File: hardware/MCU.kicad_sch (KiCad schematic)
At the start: 0 parts

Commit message: Schematic for the MCU and Tag Connect
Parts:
- added C14: 100nF, symbol Device:C
- added C15: 4.7uF, symbol Device:C
- added J2: SWD Debug, symbol Connector_Generic:Conn_01x06
- added R5: 10k, symbol Device:R
- added SW1: SW_Push, symbol Switch:SW_Push
- added U3: STM32G071KBUxN, Package_DFN_QFN:QFN-32-1EP_5x5mm_P0.5mm_EP3.45x3.45mm, symbol MCU_ST_STM32G0:STM32G071KBUxN
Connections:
- new net: SW1.2, U3.6 (PF2)
- new net: C14.2, C15.1
- new net 3V3: C14.1, J2.1 (Pin_1), U3.4 (VDD)
- new net EN_RAILB: U3.15 (PB0)
- new net GND: C15.2, J2.3 (Pin_3), J2.5 (Pin_5), R5.2, SW1.1, U3.33 (VSS), U3.5 (VSS)
- new net I2C1_SCL: U3.19 (PA9/UCPD1_DBCC1)
- new net I2C1_SDA: U3.21 (PA10/UCPD1_DBCC2)
- new net SWCLK_BOOT0: J2.4 (Pin_4), R5.1, U3.25 (PA14)
- new net SWDIO: J2.2 (Pin_2), U3.24 (PA13)
- new net USART2_RX: U3.10 (PA3)
- new net USART2_TX: U3.9 (PA2)

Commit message: Schematics Completed
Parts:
- removed J2: SWD Debug, symbol Connector_Generic:Conn_01x06

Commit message: Completed Schematic
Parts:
- added C16: 100nF, symbol Device:C
- added D2: STATUS_G, symbol Device:LED
- added D3: ERROR_R, symbol Device:LED
- added R10, R11: 470, symbol Device:R
- added R9: 10k, symbol Device:R
- renumbered R5 to R6
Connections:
- net 3V3: now also R9.2
- net GND: now also C16.2, D2.1 (K), D3.1 (K)
- net RESET: now reaches SW1.2, U3.6 (PF2)
- net RESET: now also C16.1, R9.1
- net at U3.12 (PA5): now also R10.1
- net at U3.13 (PA6): now also R11.1
- new net: D3.2 (A), R11.2
- new net: D2.2 (A), R10.2
- no-connect marks 0 -> 20
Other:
- moved on the sheet: C14, C15, R6, SW1, U3

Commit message: Assigned Footprints and Libraries
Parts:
- C14, C15, C16: footprint (none) -> Capacitor_SMD:C_0603_1608Metric
- D2, D3: footprint (none) -> LED_SMD:LED_0201_0603Metric
- R10, R11, R6, R9: footprint (none) -> Resistor_SMD:R_0201_0603Metric
- SW1: footprint (none) -> Button_Switch_SMD:SW_SPST_EVQP2_MiddlePushTravel_H2.5mm
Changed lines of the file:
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@@
 			)
 		)
-		(property "Footprint" ""
+		(property "Footprint" "Resistor_SMD:R_0201_0603Metric"
 			(at 188.722 113.03 90)
 			(hide yes)
@@
 			)
 		)
-		(property "Footprint" ""
+		(property "Footprint" "Resistor_SMD:R_0201_0603Metric"
 			(at 203.2 94.488 90)
 			(hide yes)
@@
 			)
 		)
-		(property "Footprint" ""
+		(property "Footprint" "Resistor_SMD:R_0201_0603Metric"
 			(at 203.2 84.328 90)
 			(hide yes)
@@
 			)
 		)
-		(property "Footprint" ""
+		(property "Footprint" "Button_Switch_SMD:SW_SPST_EVQP2_MiddlePushTravel_H2.5mm"
 			(at 102.87 68.58 0)
 			(hide yes)
@@
 			)
 		)
-		(property "Footprint" ""
+		(property "Footprint" "Capacitor_SMD:C_0603_1608Metric"
 			(at 172.72 54.9148 0)
 			(hide yes)
@@
 			)
 		)
-		(property "Footprint" ""
+		(property "Footprint" "Capacitor_SMD:C_0603_1608Metric"
 			(at 112.7252 82.55 0)
 			(hide yes)
@@
 			)
 		)
-		(property "Footprint" ""
+		(property "Footprint" "Resistor_SMD:R_0201_0603Metric"
 			(at 126.238 64.77 90)
 			(hide yes)
@@
 			)
 		)
-		(property "Footprint" ""
+		(property "Footprint" "Capacitor_SMD:C_0603_1608Metric"
 			(at 181.61 54.9148 0)
 			(hide yes)
@@
 			)
 		)
-		(property "Footprint" ""
+		(property "Footprint" "LED_SMD:LED_0201_0603Metric"
 			(at 212.09 82.55 0)
 			(hide yes)
@@
 			)
 		)
-		(property "Footprint" ""
+		(property "Footprint" "LED_SMD:LED_0201_0603Metric"
 			(at 212.09 92.71 0)
 			(hide yes)

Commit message: Update MCU with different enable pin
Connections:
- net EN_RAILB: now also U3.23 (PA10/PA12); no longer U3.15 (PB0)
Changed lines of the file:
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@@
-	)
-	(no_connect
-		(at 186.69 101.6)
 	)
 	(no_connect
@@
 	)
 	(no_connect
+		(at 135.89 101.6)
+	)
+	(no_connect
 		(at 135.89 104.14)
 	)
@@
 	(wire
 		(pts
-			(xy 190.5 100.33) (xy 190.5 99.06)
-		)
-		(stroke
-			(width 0)
-			(type default)
-		)
-	)
-	(wire
-		(pts
 			(xy 215.9 82.55) (xy 219.71 82.55)
 		)
@@
 	(wire
 		(pts
-			(xy 128.27 101.6) (xy 135.89 101.6)
-		)
-		(stroke
-			(width 0)
-			(type default)
-		)
-	)
-	(wire
-		(pts
 			(xy 111.76 74.93) (xy 111.76 73.66)
 		)
@@
 	(wire
 		(pts
-			(xy 190.5 100.33) (xy 195.58 100.33)
-		)
-		(stroke
-			(width 0)
-			(type default)
-		)
-	)
-	(wire
-		(pts
 			(xy 111.76 83.82) (xy 111.76 82.55)
 		)
@@
 	(wire
 		(pts
+			(xy 186.69 101.6) (xy 209.55 101.6)
+		)
+		(stroke
+			(width 0)
+			(type default)
+		)
+	)
+	(wire
+		(pts
 			(xy 207.01 92.71) (xy 208.28 92.71)
 		)
@@
 	(wire
 		(pts
-			(xy 186.69 99.06) (xy 190.5 99.06)
+			(xy 186.69 99.06) (xy 195.58 99.06)
 		)
 		(stroke
@@
 	(hierarchical_label "I2C1_SCL"
 		(shape input)
-		(at 195.58 100.33 0)
+		(at 195.58 99.06 0)
 		(effects
 			(font
@@
 		)
 	)
+	(hierarchical_label "EN_RAILB"
+		(shape input)
+		(at 209.55 101.6 0)
+		(effects
+			(font
+				(size 1.27 1.27)
+			)
+			(justify left)
+		)
+	)
 	(hierarchical_label "SWDIO"
 		(shape output)
@@
 		(effects
 			(font
-				(size 1.27 1.27)
-			)
-			(justify right)
-		)
-	)
-	(hierarchical_label "EN_RAILB"
-		(shape input)
-		(at 128.27 101.6 180)
-		(effects
-			(font

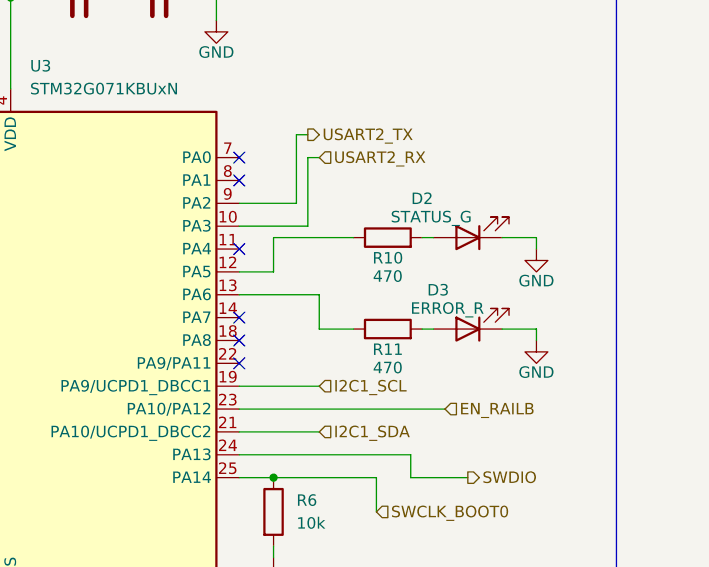
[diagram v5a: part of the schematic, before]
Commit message: LED circuit change
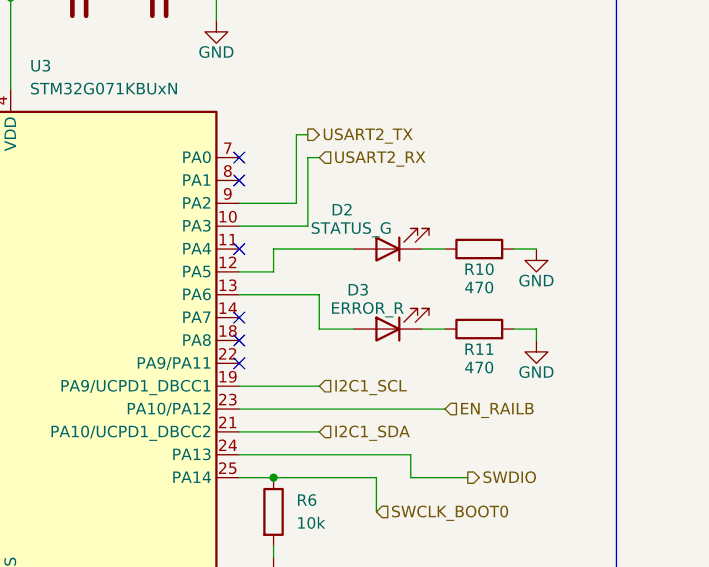
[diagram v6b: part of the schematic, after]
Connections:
- net GND: now also R10.2, R11.2; no longer D2.1 (K), D3.1 (K)
- net at R11.1: now also D3.1 (K); no longer U3.13 (PA6)
- net at D3.2 (A): now also U3.13 (PA6); no longer R11.2
- net at R10.1: now also D2.1 (K); no longer U3.12 (PA5)
- net at D2.2 (A): now also U3.12 (PA5); no longer R10.2
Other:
- moved on the sheet: R10, R11

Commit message: PCB V1.1
Board completed, updated with labels for external connectors. Corrected and tightened hot loop with better layout and routing
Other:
- moved on the sheet: D3, R11
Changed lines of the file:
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@@
 	(paper "A4")
 	(rectangle
-		(start 76.2 41.91)
-		(end 228.6 139.7)
+		(start 77.47 40.64)
+		(end 229.87 138.43)
 		(stroke
 			(width 0)
@@
 	(wire
 		(pts
+			(xy 190.5 88.9) (xy 186.69 88.9)
+		)
+		(stroke
+			(width 0)
+			(type default)
+		)
+	)
+	(wire
+		(pts
 			(xy 111.76 74.93) (xy 111.76 73.66)
 		)
@@
 	(wire
 		(pts
-			(xy 219.71 92.71) (xy 219.71 93.98)
+			(xy 219.71 91.44) (xy 219.71 92.71)
 		)
 		(stroke
@@
 	(wire
 		(pts
-			(xy 186.69 88.9) (xy 195.58 88.9)
-		)
-		(stroke
-			(width 0)
-			(type default)
-		)
-	)
-	(wire
-		(pts
 			(xy 212.09 109.22) (xy 205.74 109.22)
 		)
@@
 	(wire
 		(pts
-			(xy 207.01 92.71) (xy 209.55 92.71)
-		)
-		(stroke
-			(width 0)
-			(type default)
-		)
-	)
-	(wire
-		(pts
-			(xy 195.58 88.9) (xy 195.58 92.71)
+			(xy 207.01 91.44) (xy 209.55 91.44)
+		)
+		(stroke
+			(width 0)
+			(type default)
+		)
+	)
+	(wire
+		(pts
+			(xy 190.5 88.9) (xy 190.5 91.44)
 		)
 		(stroke
@@
 	(wire
 		(pts
-			(xy 217.17 92.71) (xy 219.71 92.71)
+			(xy 217.17 91.44) (xy 219.71 91.44)
 		)
 		(stroke
@@
 	(wire
 		(pts
-			(xy 194.31 73.66) (xy 194.31 81.28)
+			(xy 193.04 73.66) (xy 193.04 81.28)
 		)
 		(stroke
@@
 	(wire
 		(pts
+			(xy 219.71 85.09) (xy 219.71 83.82)
+		)
+		(stroke
+			(width 0)
+			(type default)
+		)
+	)
+	(wire
+		(pts
 			(xy 184.15 55.88) (xy 184.15 58.42)
 		)
@@
 	(wire
 		(pts
-			(xy 195.58 92.71) (xy 199.39 92.71)
-		)
-		(stroke
-			(width 0)
-			(type default)
-		)
-	)
-	(wire
-		(pts
-			(xy 193.04 78.74) (xy 186.69 78.74)
-		)
-		(stroke
-			(width 0)
-			(type default)
-		)
-	)
-	(wire
-		(pts
-			(xy 193.04 71.12) (xy 194.31 71.12)
-		)
-		(stroke
-			(width 0)
-			(type default)
-		)
-	)
-	(wire
-		(pts
-			(xy 193.04 71.12) (xy 193.04 78.74)
+			(xy 190.5 91.44) (xy 199.39 91.44)
+		)
+		(stroke
+			(width 0)
+			(type default)
+		)
+	)
+	(wire
+		(pts
+			(xy 191.77 78.74) (xy 186.69 78.74)
+		)
+		(stroke
+			(width 0)
+			(type default)
+		)
+	)
+	(wire
+		(pts
+			(xy 191.77 71.12) (xy 194.31 71.12)
+		)
+		(stroke
+			(width 0)
+			(type default)
+		)
+	)
+	(wire
+		(pts
+			(xy 191.77 71.12) (xy 191.77 78.74)
 		)
 		(stroke
@@
 	(wire
 		(pts
-			(xy 194.31 73.66) (xy 195.58 73.66)
+			(xy 193.04 73.66) (xy 195.58 73.66)
 		)
 		(stroke
@@
 	(wire
 		(pts
-			(xy 194.31 81.28) (xy 186.69 81.28)
-		)
-		(stroke
-			(width 0)
-			(type default)
-		)
-	)
-	(wire
-		(pts
-			(xy 217.17 83.82) (xy 219.71 83.82)
+			(xy 193.04 81.28) (xy 186.69 81.28)
+		)
+		(stroke
+			(width 0)
+			(type default)
+		)
+	)
+	(wire
+		(pts
+			(xy 219.71 83.82) (xy 217.17 83.82)
 		)
 		(stroke
@@
 	(symbol
 		(lib_id "Device:LED")
-		(at 203.2 92.71 180)
+		(at 203.2 91.44 180)
 		(unit 1)
 		(body_style 1)
@@
 		(dnp no)
 		(property "Reference" "D3"
-			(at 199.898 88.392 0)
+			(at 199.898 87.122 0)
 			(show_name no)
 			(do_not_autoplace no)
@@
 		)
 		(property "Value" "ERROR_R"
-			(at 200.914 90.424 0)
+			(at 200.914 89.154 0)
 			(show_name no)
 			(do_not_autoplace no)
@@
 		)
 		(property "Footprint" "LED_SMD:LED_0201_0603Metric"
-			(at 203.2 92.71 0)
+			(at 203.2 91.44 0)
 			(hide yes)
 			(show_name no)
@@
 		)
 		(property "Datasheet" ""
-			(at 203.2 92.71 0)
+			(at 203.2 91.44 0)
 			(hide yes)
 			(show_name no)
@@
 		)
 		(property "Description" "Light emitting diode"
-			(at 203.2 92.71 0)
+			(at 203.2 91.44 0)
 			(hide yes)
 			(show_name no)
@@
 		)
 		(property "Sim.Pins" "1=K 2=A"
-			(at 203.2 92.71 0)
+			(at 203.2 91.44 0)
 			(hide yes)
 			(show_name no)
@@
 	(symbol
 		(lib_id "power:GND")
-		(at 219.71 83.82 0)
+		(at 219.71 85.09 0)
 		(unit 1)
 		(body_style 1)
@@
 		(dnp no)
 		(property "Reference" "#PWR021"
-			(at 219.71 90.17 0)
+			(at 219.71 91.44 0)
 			(hide yes)
 			(show_name no)
@@
 		)
 		(property "Value" "GND"
-			(at 219.71 87.376 0)
+			(at 219.71 88.646 0)
 			(show_name no)
 			(do_not_autoplace no)
@@
 		)
 		(property "Footprint" ""
-			(at 219.71 83.82 0)
+			(at 219.71 85.09 0)
 			(hide yes)
 			(show_name no)
@@
 		)
 		(property "Datasheet" ""
-			(at 219.71 83.82 0)
+			(at 219.71 85.09 0)
 			(hide yes)
 			(show_name no)
@@
 		)
 		(property "Description" "Power symbol creates a global label with name \"GND\" , ground"
-			(at 219.71 83.82 0)
+			(at 219.71 85.09 0)
 			(hide yes)
 			(show_name no)
@@
 	(symbol
 		(lib_id "Device:R")
-		(at 213.36 92.71 90)
+		(at 213.36 91.44 90)
 		(unit 1)
 		(body_style 1)
@@
 		(dnp no)
 		(property "Reference" "R11"
-			(at 213.36 94.996 90)
+			(at 213.36 93.726 90)
 			(show_name no)
 			(do_not_autoplace no)
@@
 		)
 		(property "Value" "470"
-			(at 213.36 97.028 90)
+			(at 213.36 95.758 90)
 			(show_name no)
 			(do_not_autoplace no)
@@
 		)
 		(property "Footprint" "Resistor_SMD:R_0201_0603Metric"
-			(at 213.36 94.488 90)
+			(at 213.36 93.218 90)
 			(hide yes)
 			(show_name no)
@@
 		)
 		(property "Datasheet" ""
-			(at 213.36 92.71 0)
+			(at 213.36 91.44 0)
 			(hide yes)
 			(show_name no)
@@
 		)
 		(property "Description" "Resistor"
-			(at 213.36 92.71 0)
+			(at 213.36 91.44 0)
 			(hide yes)
 			(show_name no)
@@
 	(symbol
 		(lib_id "power:GND")
-		(at 219.71 93.98 0)
+		(at 219.71 92.71 0)
 		(unit 1)
 		(body_style 1)
@@
 		(dnp no)
 		(property "Reference" "#PWR022"
-			(at 219.71 100.33 0)
+			(at 219.71 99.06 0)
 			(hide yes)
 			(show_name no)
@@
 		)
 		(property "Value" "GND"
-			(at 219.71 97.536 0)
+			(at 219.71 96.266 0)
 			(show_name no)
 			(do_not_autoplace no)
@@
 		)
 		(property "Footprint" ""
-			(at 219.71 93.98 0)
+			(at 219.71 92.71 0)
 			(hide yes)
 			(show_name no)
@@
 		)
 		(property "Datasheet" ""
-			(at 219.71 93.98 0)
+			(at 219.71 92.71 0)
 			(hide yes)
 			(show_name no)
@@
 		)
 		(property "Description" "Power symbol creates a global label with name \"GND\" , ground"
-			(at 219.71 93.98 0)
-			(hide yes)
-			(show_name no)
+			(at 219.71 92.71 0)
+			(hide yes)
+			(show_name no)
